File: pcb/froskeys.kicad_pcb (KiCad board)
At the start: 2 copper layers, 81 x 86.3 mm, 30 parts, among them J1 OLED, SW1 MX, SW10 RotaryEncoder_Switch, SW2 MX, SW3 MX, SW4 MX, SW5 MX, SW6 MX, SW7 MX, SW8 MX, SW9 MX, U1 XIAO-RP2040-DIP

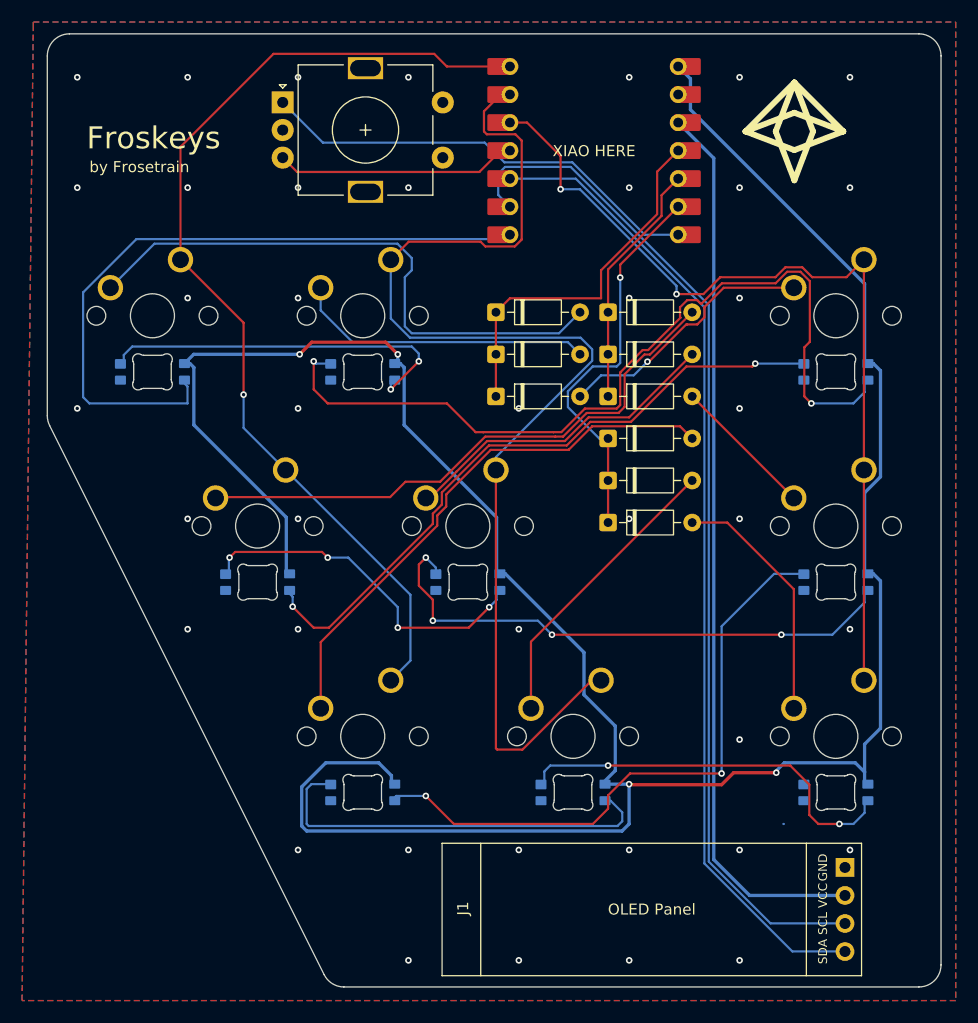
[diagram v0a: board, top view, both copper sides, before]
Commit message: Change SK6812 pin order
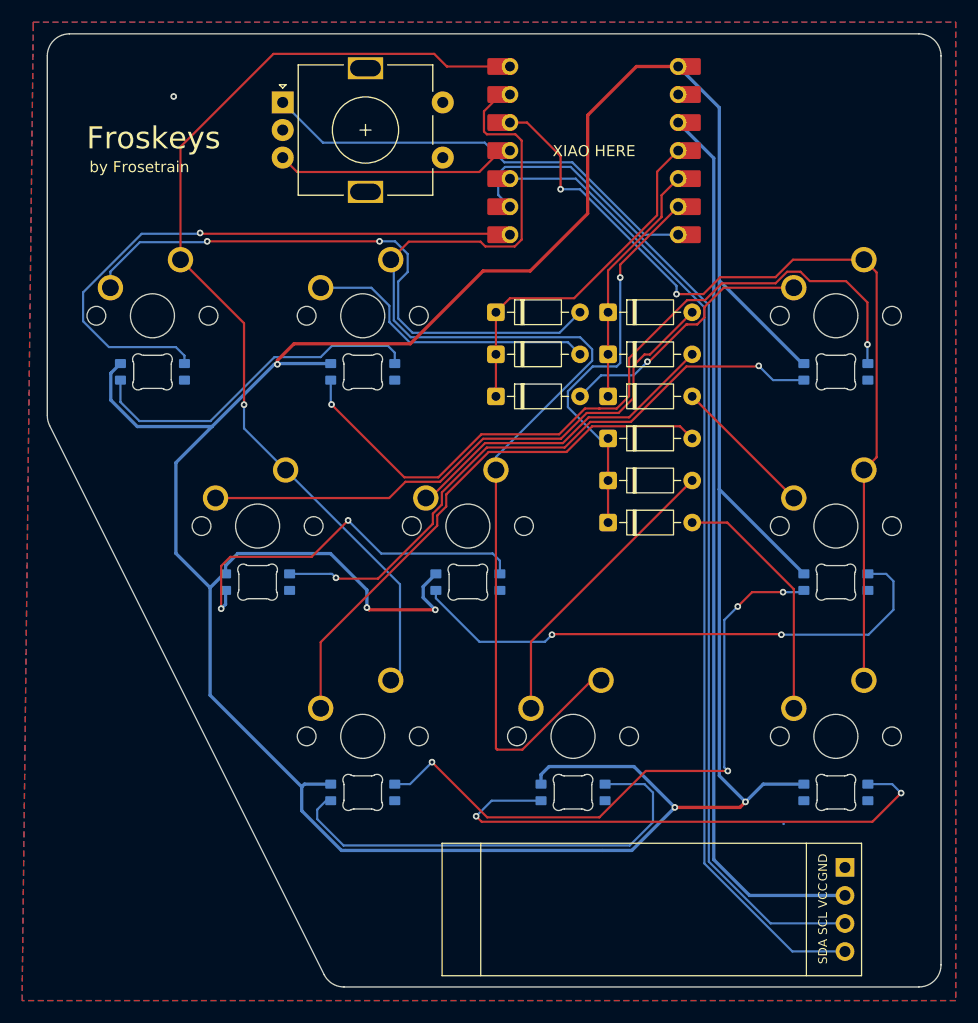
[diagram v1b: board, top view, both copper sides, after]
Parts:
- added KICAD: KiCad-Logo2_6mm_Copper, Symbol:KiCad-Logo2_6mm_Copper, F.Cu at (143.5, 134.0)
- added OSHW: OSHW-Logo_7.5x8mm_Copper, Symbol:OSHW-Logo_7.5x8mm_Copper, B.Cu at (143.5, 134.6)
- LED1, LED2, LED3, LED4, LED5, LED6, LED7, LED8, LED9: footprint Keyboard Parts:MX_SK6812MINI-E -> Keyboard Parts:MX_SK6812MINI-E_GOOD
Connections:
- LED1 pad 1: Net-(LED1-DOUT) -> GND
- LED1 pad 2: GND -> DIN
- LED1 pad 3: DIN -> +5V
- LED1 pad 4: +5V -> Net-(LED1-DOUT)
- LED2 pad 1: Net-(LED2-DOUT) -> GND
- LED2 pad 2: GND -> Net-(LED1-DOUT)
- LED2 pad 3: Net-(LED1-DOUT) -> +5V
- LED2 pad 4: +5V -> Net-(LED2-DOUT)
- LED3 pad 1: Net-(LED3-DOUT) -> GND
- LED3 pad 2: GND -> Net-(LED2-DOUT)
- LED3 pad 3: Net-(LED2-DOUT) -> +5V
- LED3 pad 4: +5V -> Net-(LED3-DOUT)
- LED4 pad 1: Net-(LED4-DOUT) -> GND
- LED4 pad 2: GND -> Net-(LED3-DOUT)
- LED4 pad 3: Net-(LED3-DOUT) -> +5V
- LED4 pad 4: +5V -> Net-(LED4-DOUT)
- LED5 pad 1: Net-(LED5-DOUT) -> GND
- LED5 pad 2: GND -> Net-(LED4-DOUT)
- LED5 pad 3: Net-(LED4-DOUT) -> +5V
- LED5 pad 4: +5V -> Net-(LED5-DOUT)
- LED6 pad 1: Net-(LED6-DOUT) -> GND
- LED6 pad 2: GND -> Net-(LED5-DOUT)
- LED6 pad 3: Net-(LED5-DOUT) -> +5V
- LED6 pad 4: +5V -> Net-(LED6-DOUT)
- LED7 pad 1: Net-(LED7-DOUT) -> GND
- LED7 pad 2: GND -> Net-(LED6-DOUT)
- LED7 pad 3: Net-(LED6-DOUT) -> +5V
- LED7 pad 4: +5V -> Net-(LED7-DOUT)
- LED8 pad 1: Net-(LED8-DOUT) -> GND
- LED8 pad 2: GND -> Net-(LED7-DOUT)
- LED8 pad 3: Net-(LED7-DOUT) -> +5V
- LED8 pad 4: +5V -> Net-(LED8-DOUT)
- LED9 pad 1: unconnected-(LED9-DOUT-Pad1) -> GND
- LED9 pad 2: GND -> Net-(LED8-DOUT)
- LED9 pad 3: Net-(LED8-DOUT) -> +5V
- LED9 pad 4: +5V -> unconnected-(LED9-DOUT-Pad4)
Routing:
- net +5V: track 241.6 -> 307.7 mm, vias 4 -> 5
- net Net-(LED8-DOUT): track 35.7 -> 49.6 mm
- net Net-(LED2-DOUT): track 77.9 -> 70.0 mm
- net DIN: track 62.4 -> 54.8 mm, vias 0 -> 1
- net Net-(LED7-DOUT): track 37.8 -> 42.1 mm
- net Net-(LED3-DOUT): track 60.2 -> 56.5 mm
- net Net-(LED4-DOUT): track 31.7 -> 35.4 mm, vias 4 -> 2
- net Net-(LED1-DOUT): track 33.2 -> 31.6 mm, vias 2 -> 0
- net ROW1: track 33.9 -> 32.5 mm
- net Net-(D1-A): track 52.9 -> 54.0 mm, vias 0 -> 2
- net COL1: track 91.6 -> 90.8 mm
- net Net-(LED5-DOUT): track 50.8 -> 50.2 mm, vias 4 -> 2
- net Net-(LED6-DOUT): track 56.8 -> 56.9 mm, vias 2 -> 4
- net GND: vias 41 -> 1

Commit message: Oops add stitching vias
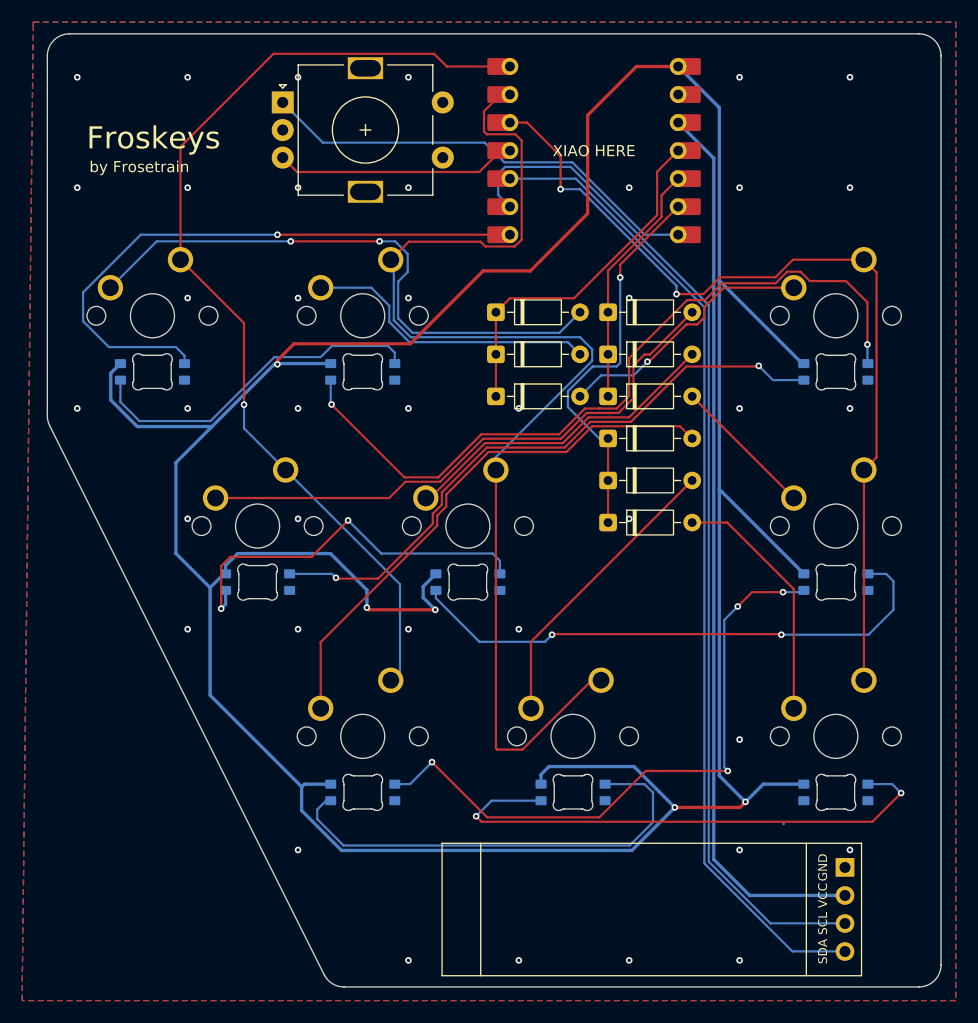
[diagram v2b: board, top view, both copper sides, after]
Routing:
- net Net-(D1-A): track 54.0 -> 53.1 mm
- net GND: vias 1 -> 39
